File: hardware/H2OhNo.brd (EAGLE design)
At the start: 44.5 x 22.9 mm, 12 parts, among them U2 TINY85-20-DIP

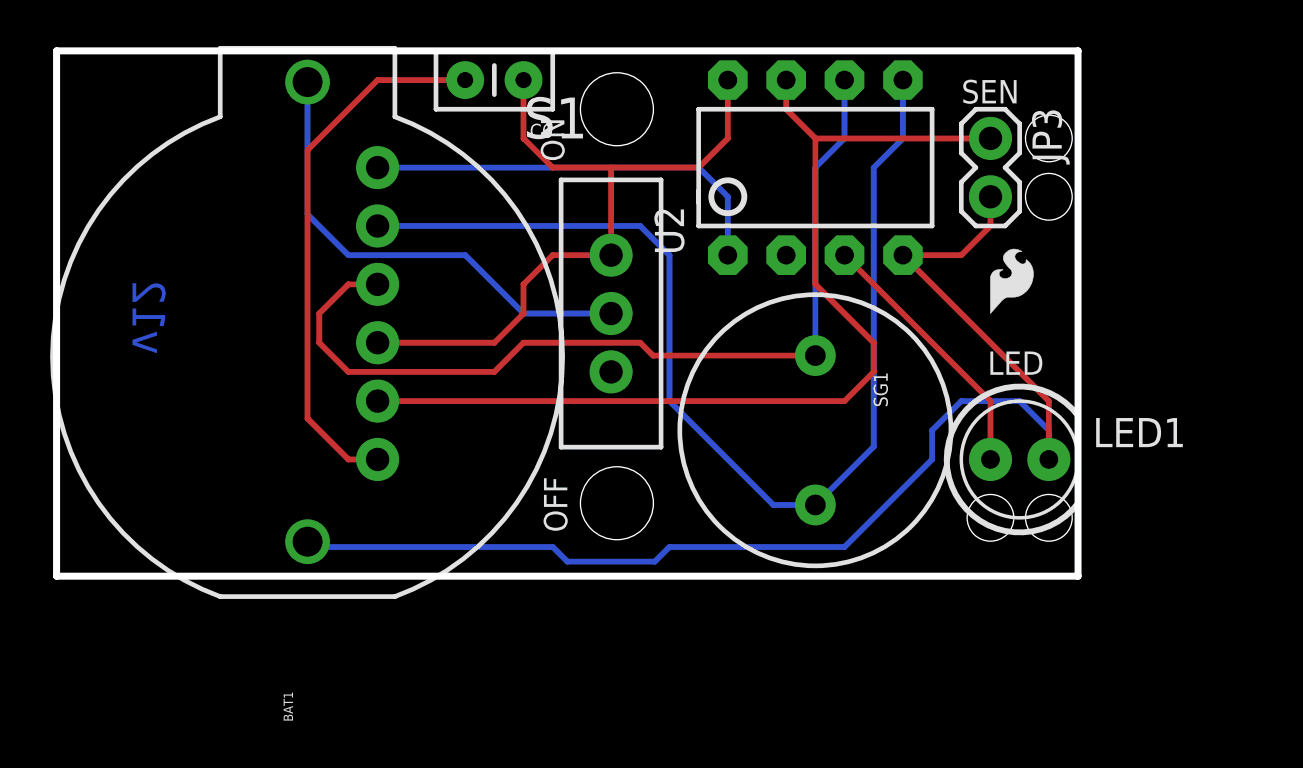
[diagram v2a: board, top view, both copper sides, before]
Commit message: Hardware changes to address issues on github.
Moved 0.1uF cap closer to IC. Added standoffs. Increased board size.
Moved LED and sense towards end of board.
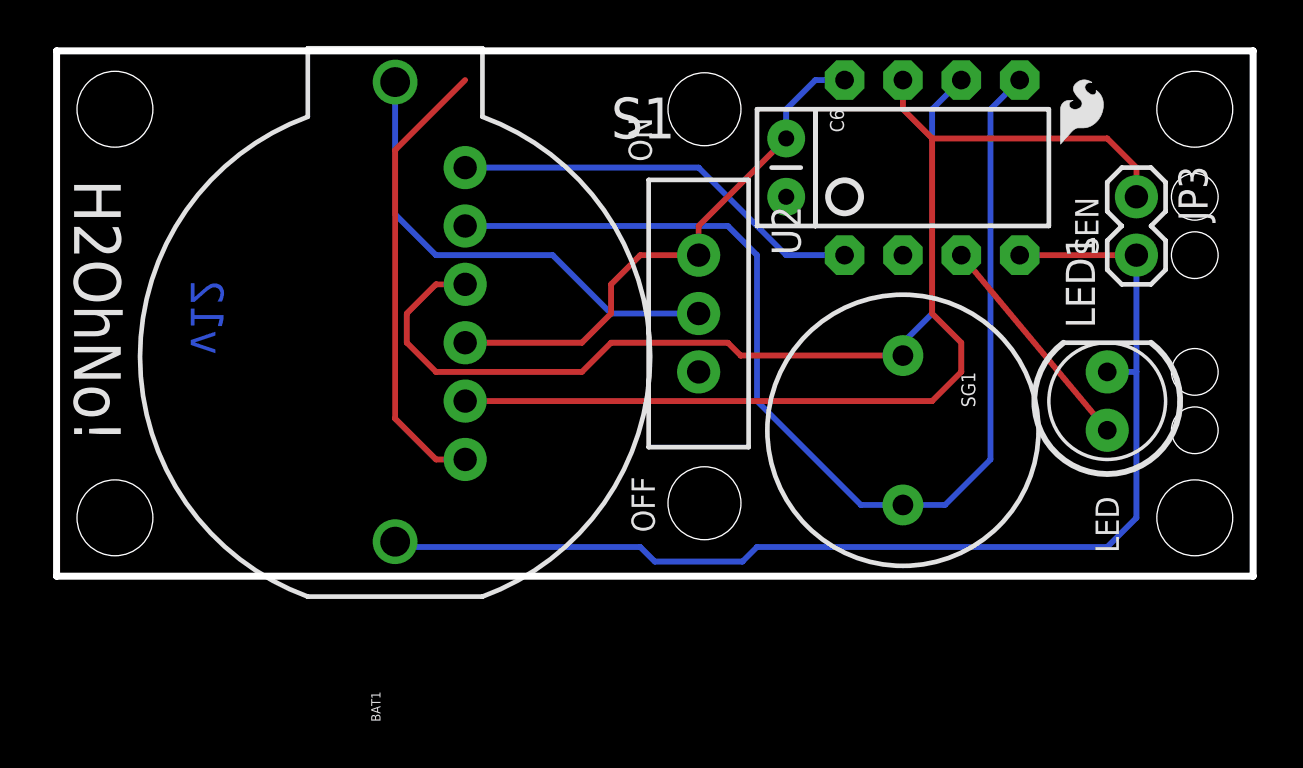
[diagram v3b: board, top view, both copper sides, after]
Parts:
- removed U$2: CREATIVE_COMMONS, SparkFun:CREATIVE_COMMONS
- added FRAME2: FRAME-LETTER, SparkFun-Aesthetics:CREATIVE_COMMONS
- added STANDOFF1, STANDOFF2, STANDOFF3, STANDOFF4: STAND-OFF, SparkFun-Electromechanical:STAND-OFF
- JP4: value (none) -> ISP
- SG1: value BUZZERPTH -> Buzzer
- moved C6 11.7 mm to (31.8, 19.1), turned to 270 degrees
- moved U$1 7.97 mm to (43.7, 18.8)
- moved JP3 6.84 mm to (47.0, 16.5)
- moved U2 5.08 mm to (38.1, 17.8)
- moved LED1 4.58 mm to (45.7, 7.62), turned to 90 degrees
- moved S1 3.81 mm to (27.9, 11.4)
- moved JP4 3.81 mm to (17.8, 17.8)
- moved BAT1 3.81 mm to (14.7, 9.65)
- moved U$4 3.81 mm to (24.1, 11.4)
- moved SG1 3.81 mm to (36.8, 6.35)
- moved U$5 2.54 mm to (7.49, 5.33)
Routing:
- net VCC: track 31.3 -> 23.5 mm
- net GND: track 78.5 -> 70.7 mm
- net D2: track 44.0 -> 46.6 mm
- net D4: track 11.5 -> 9.92 mm
- net D0: track 47.9 -> 49.5 mm
- net D1: track 39.7 -> 40.3 mm
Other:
- board size 44.5 x 22.9 mm -> 52.1 x 22.9 mm
